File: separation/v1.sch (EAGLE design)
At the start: 9 parts, among them IC1 L7805ACV

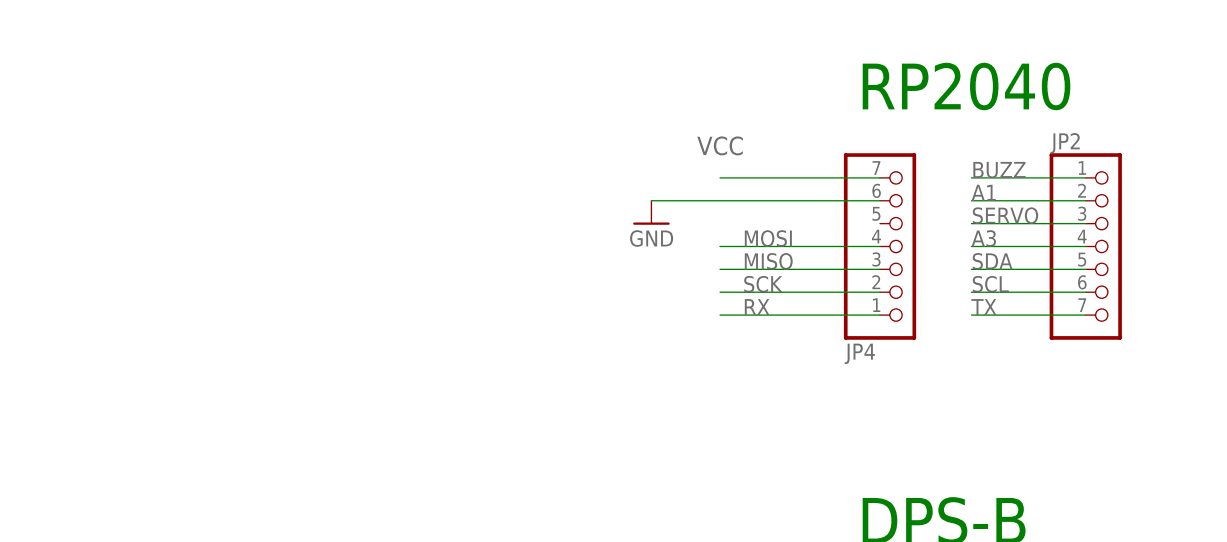
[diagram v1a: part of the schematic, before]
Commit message: add voltage divider
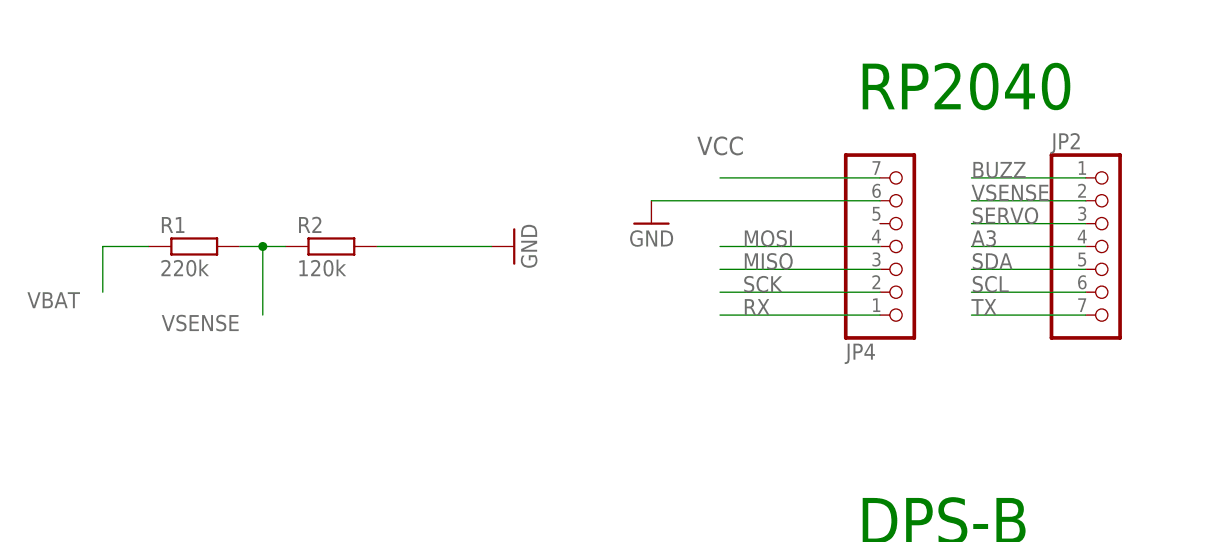
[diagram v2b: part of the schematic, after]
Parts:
- added R1: 220k, rcl:R-EU_0204/5
- added R2: 120k, rcl:R-EU_0204/5
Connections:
- removed net A1: JP2.2
- new net VSENSE: JP2.2, R1.2, R2.1
- net GND: now also R2.2
- net VBAT: now also R1.1
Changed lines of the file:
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@@
 <part name="U$4" library="microbuilder" deviceset="GND" device=""/>
 <part name="U$2" library="microbuilder" deviceset="GND" device=""/>
+<part name="R1" library="rcl" library_urn="urn:adsk.eagle:library:334" deviceset="R-EU_" device="0204/5" package3d_urn="urn:adsk.eagle:package:23488/1" value="220k"/>
+<part name="R2" library="rcl" library_urn="urn:adsk.eagle:library:334" deviceset="R-EU_" device="0204/5" package3d_urn="urn:adsk.eagle:package:23488/1" value="120k"/>
+<part name="GND4" library="supply1" library_urn="urn:adsk.eagle:library:371" deviceset="GND" device=""/>
 </parts>
 <sheets>
@@
 <attribute name="VALUE" x="15.24" y="9.144" size="1.27" layer="96" rot="R270"/>
 </instance>
+<instance part="R1" gate="G$1" x="-43.18" y="63.5" smashed="yes">
+<attribute name="NAME" x="-46.99" y="64.9986" size="1.778" layer="95"/>
+<attribute name="VALUE" x="-46.99" y="60.198" size="1.778" layer="96"/>
+</instance>
+<instance part="R2" gate="G$1" x="-27.94" y="63.5" smashed="yes">
+<attribute name="NAME" x="-31.75" y="64.9986" size="1.778" layer="95"/>
+<attribute name="VALUE" x="-31.75" y="60.198" size="1.778" layer="96"/>
+</instance>
+<instance part="GND4" gate="1" x="-7.62" y="63.5" smashed="yes" rot="MR270">
+<attribute name="VALUE" x="-5.08" y="66.04" size="1.778" layer="96" rot="MR270"/>
+</instance>
 </instances>
 <busses>
@@
 <wire x1="48.26" y1="7.62" x2="20.32" y2="7.62" width="0.1524" layer="91"/>
 </segment>
+<segment>
+<pinref part="R2" gate="G$1" pin="2"/>
+<wire x1="-22.86" y1="63.5" x2="-10.16" y2="63.5" width="0.1524" layer="91"/>
+<pinref part="GND4" gate="1" pin="GND"/>
+</segment>
 </net>
 <net name="MOSI" class="0">
@@
 </segment>
 </net>
-<net name="A1" class="0">
-<segment>
-<pinref part="JP2" gate="A" pin="2"/>
-<wire x1="55.88" y1="68.58" x2="43.18" y2="68.58" width="0.1524" layer="91"/>
-<label x="43.18" y="68.58" size="1.778" layer="95"/>
-</segment>
-</net>
 <net name="SCL" class="0">
 <segment>
@@
 <label x="33.02" y="-20.32" size="2.032" layer="95"/>
 </segment>
+<segment>
+<pinref part="R1" gate="G$1" pin="1"/>
+<wire x1="-48.26" y1="63.5" x2="-53.34" y2="63.5" width="0.1524" layer="91"/>
+<wire x1="-53.34" y1="63.5" x2="-53.34" y2="58.42" width="0.1524" layer="91"/>
+<label x="-55.88" y="58.42" size="1.778" layer="95" rot="R180"/>
+</segment>
 </net>
 <net name="BUZZ" class="0">
@@
 <pinref part="JP2" gate="A" pin="1"/>
 <wire x1="43.18" y1="71.12" x2="55.88" y2="71.12" width="0.1524" layer="91"/>
+</segment>
+</net>
+<net name="VSENSE" class="0">
+<segment>
+<pinref part="R1" gate="G$1" pin="2"/>
+<pinref part="R2" gate="G$1" pin="1"/>
+<wire x1="-38.1" y1="63.5" x2="-35.56" y2="63.5" width="0.1524" layer="91"/>
+<wire x1="-35.56" y1="63.5" x2="-33.02" y2="63.5" width="0.1524" layer="91"/>
+<wire x1="-35.56" y1="63.5" x2="-35.56" y2="55.88" width="0.1524" layer="91"/>
+<junction x="-35.56" y="63.5"/>
+<label x="-38.1" y="55.88" size="1.778" layer="95" rot="R180"/>
+</segment>
+<segment>
+<pinref part="JP2" gate="A" pin="2"/>
+<wire x1="55.88" y1="68.58" x2="43.18" y2="68.58" width="0.1524" layer="91"/>
+<label x="43.18" y="68.58" size="1.778" layer="95"/>
 </segment>
 </net>
@@
 packages will not be understood (or retained) with this version.
 </note>
+<note version="8.4" severity="warning">
+Since Version 8.4, EAGLE supports properties for SPICE simulation.
+Probes in schematics and SPICE mapping objects found in parts and library devices
+will not be understood with this version. Update EAGLE to the latest version
+for full support of SPICE simulation.
+</note>
 </compatibility>
